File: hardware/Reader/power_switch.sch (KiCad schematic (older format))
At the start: 6 parts

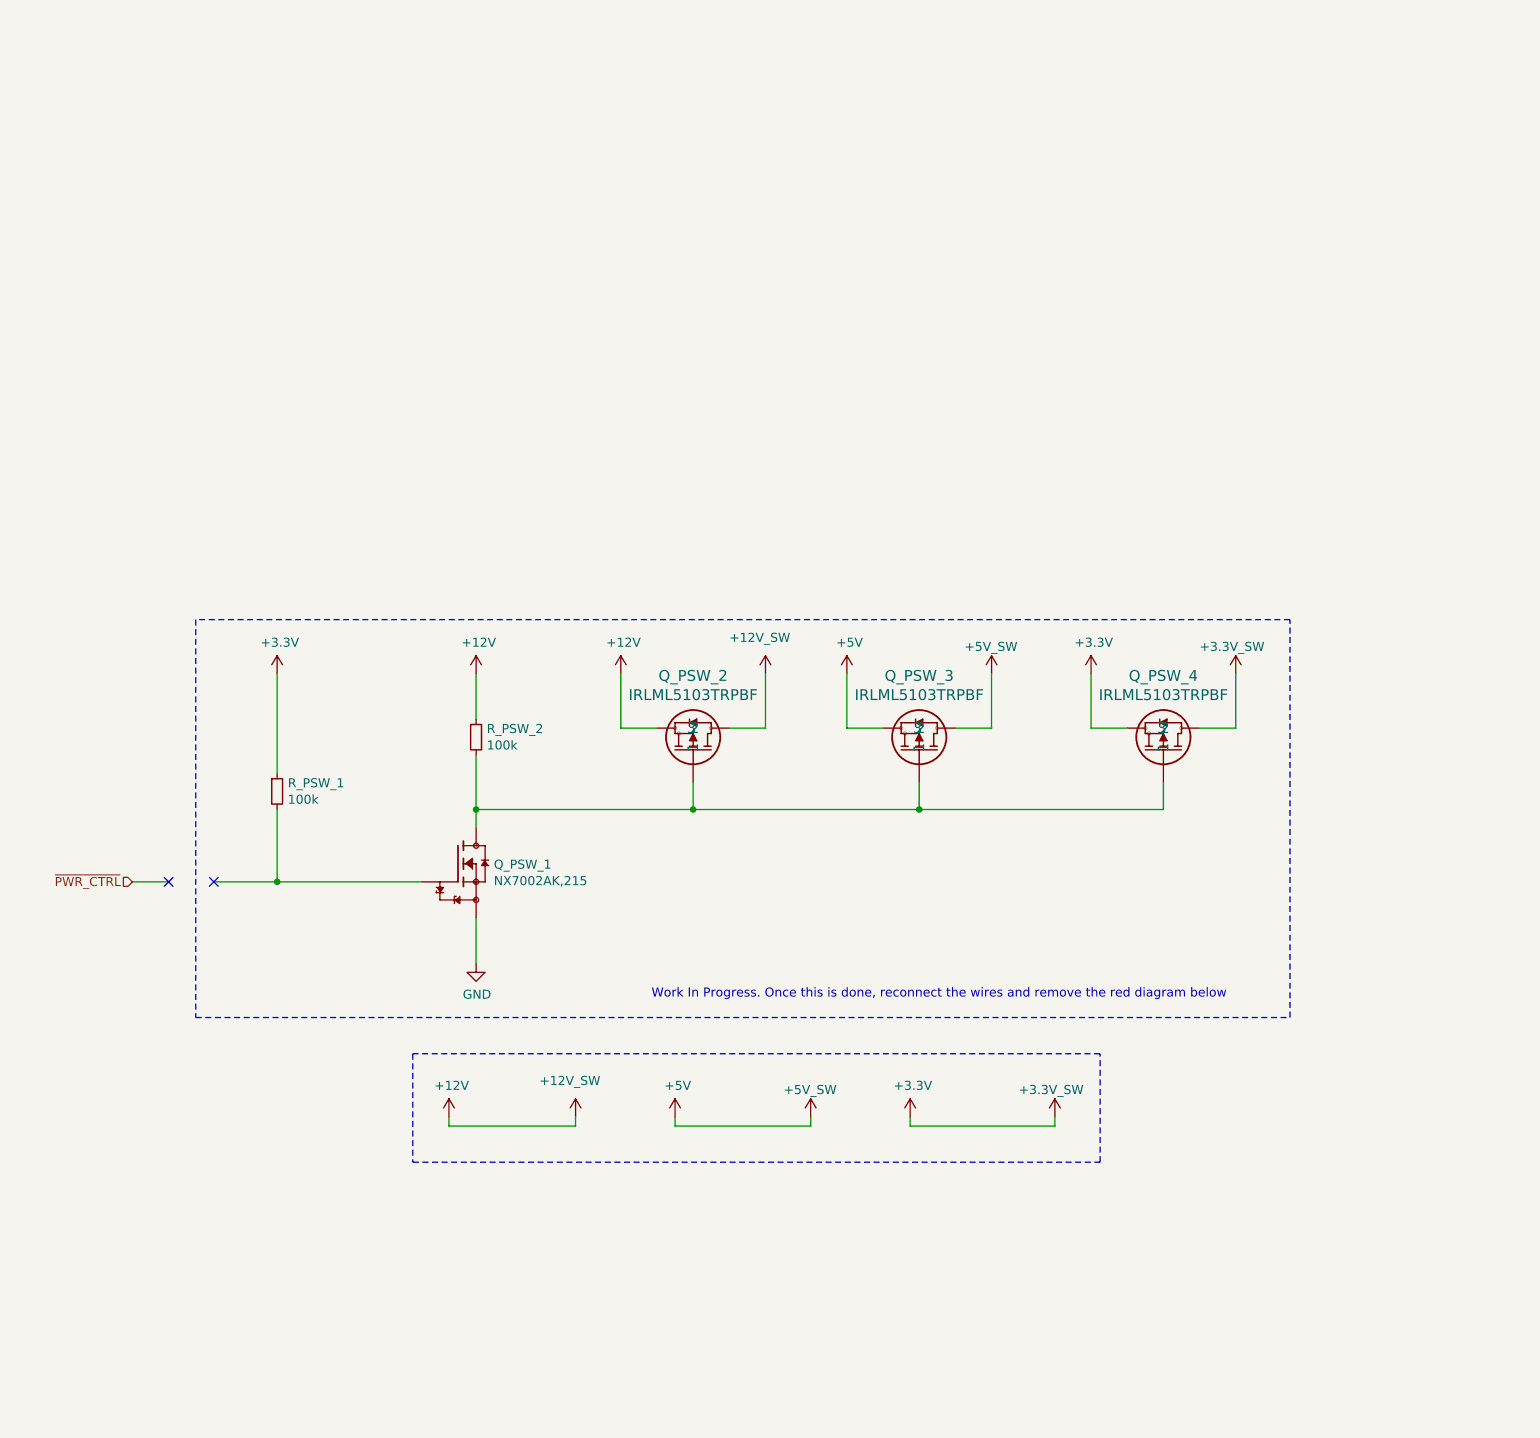
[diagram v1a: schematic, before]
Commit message: Completed Reader schematics for version 0.0.01
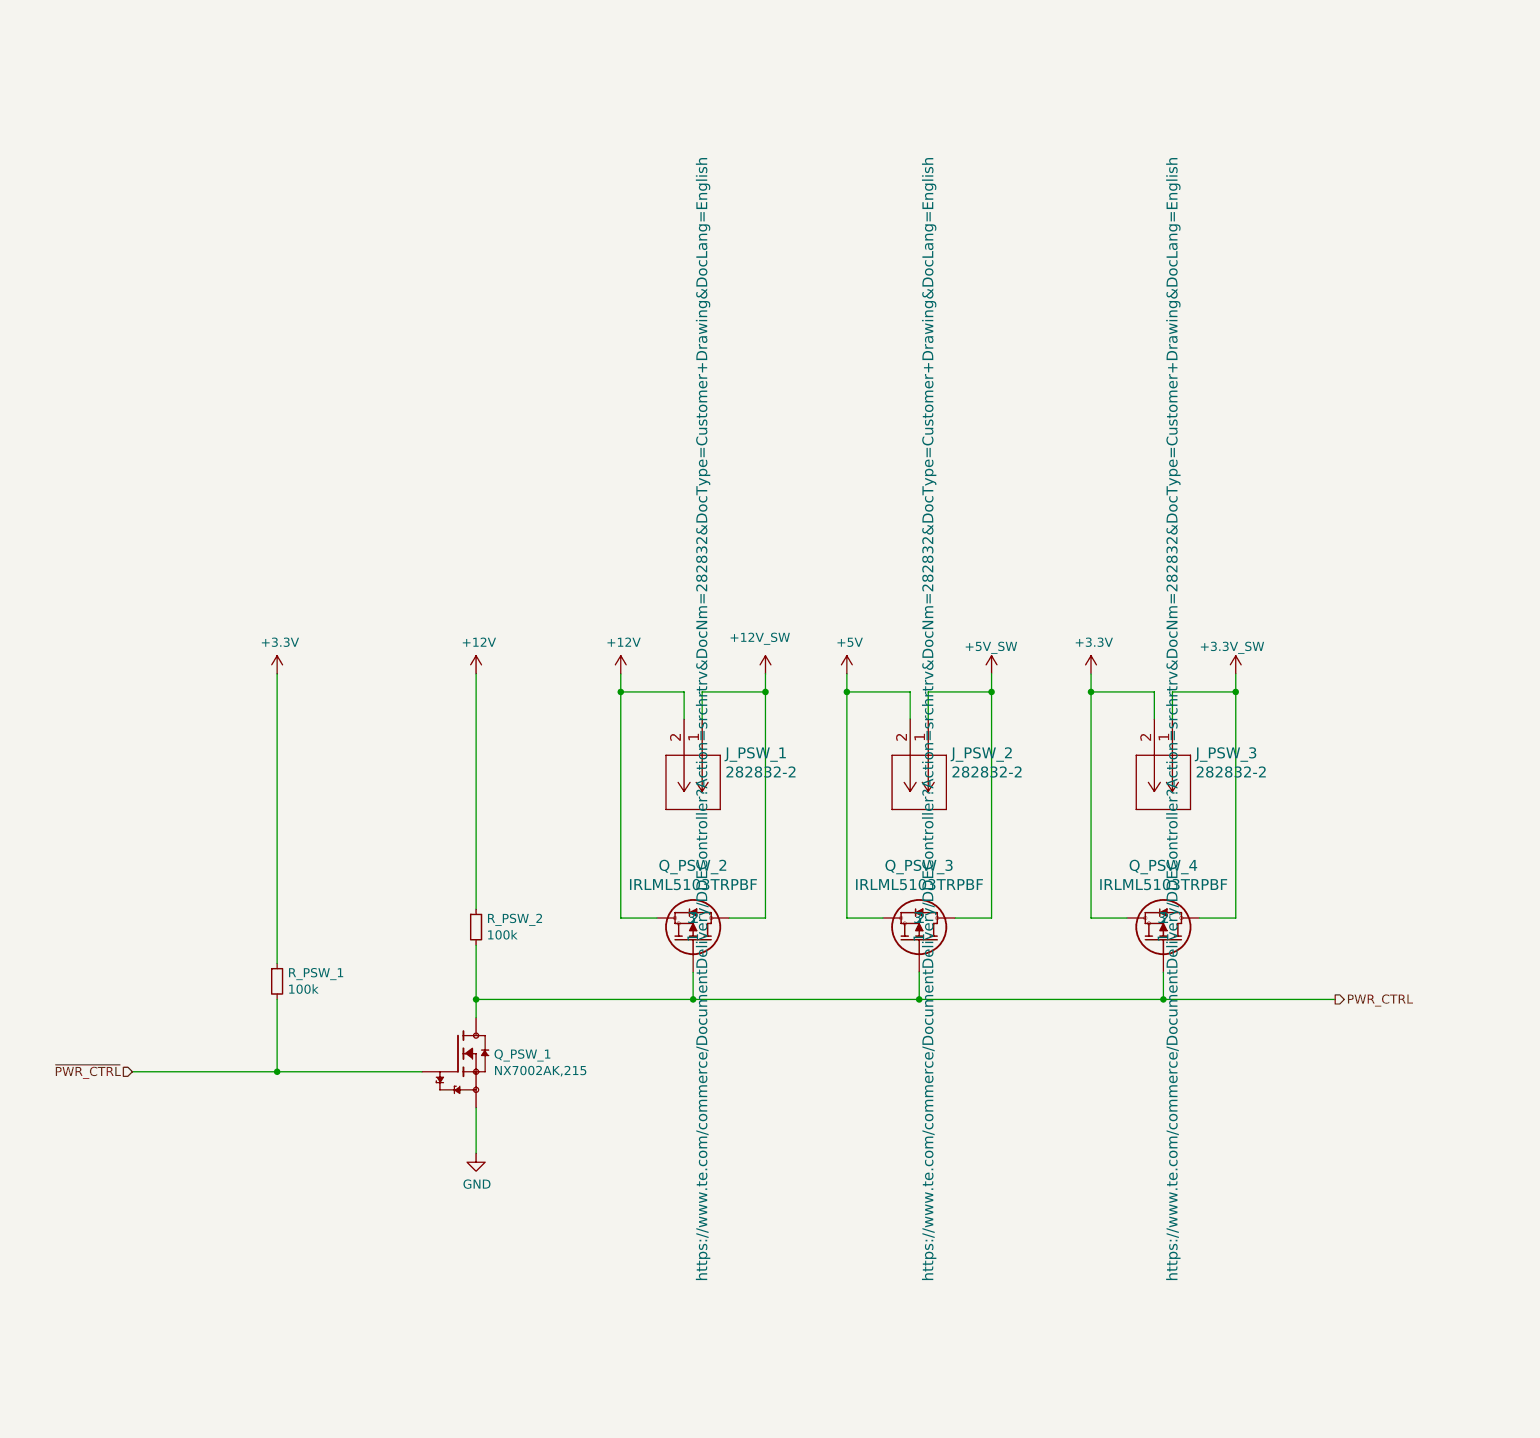
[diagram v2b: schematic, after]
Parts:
- added J_PSW_1, J_PSW_2, J_PSW_3: 282832-2, footprints:282832-2, symbol 2828322:282832-2
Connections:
- net +12V: now also J_PSW_1.2; no longer Q_PSW_2.2
- net +3.3V_SW: now also J_PSW_3.1; no longer Q_PSW_4.3, R_PSW_1.1
- net +5V: now also J_PSW_2.2; no longer Q_PSW_3.2
- net ~PWR_CTRL~: now also Q_PSW_1.1, R_PSW_1.2
- net PWR_CTRL: now reaches Q_PSW_1.3, Q_PSW_2.1, Q_PSW_3.1, Q_PSW_4.1, R_PSW_2.2
- new net +12V_SW: J_PSW_1.1, Q_PSW_2.2
- new net +3V3: J_PSW_3.2, Q_PSW_4.3, R_PSW_1.1
- new net +5V_SW: J_PSW_2.1, Q_PSW_3.2
- no-connect marks 2 -> 0
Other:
- note removed: "Work In Progress. Once this is done, reconnect the wires and remove the red diagram below"
- moved on the sheet: Q_PSW_1, Q_PSW_2, Q_PSW_3, Q_PSW_4, R_PSW_1, R_PSW_2

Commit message: Minor changes to schematic design for clarity. Added important IC datasheets. Exported schematics and rough gerber files
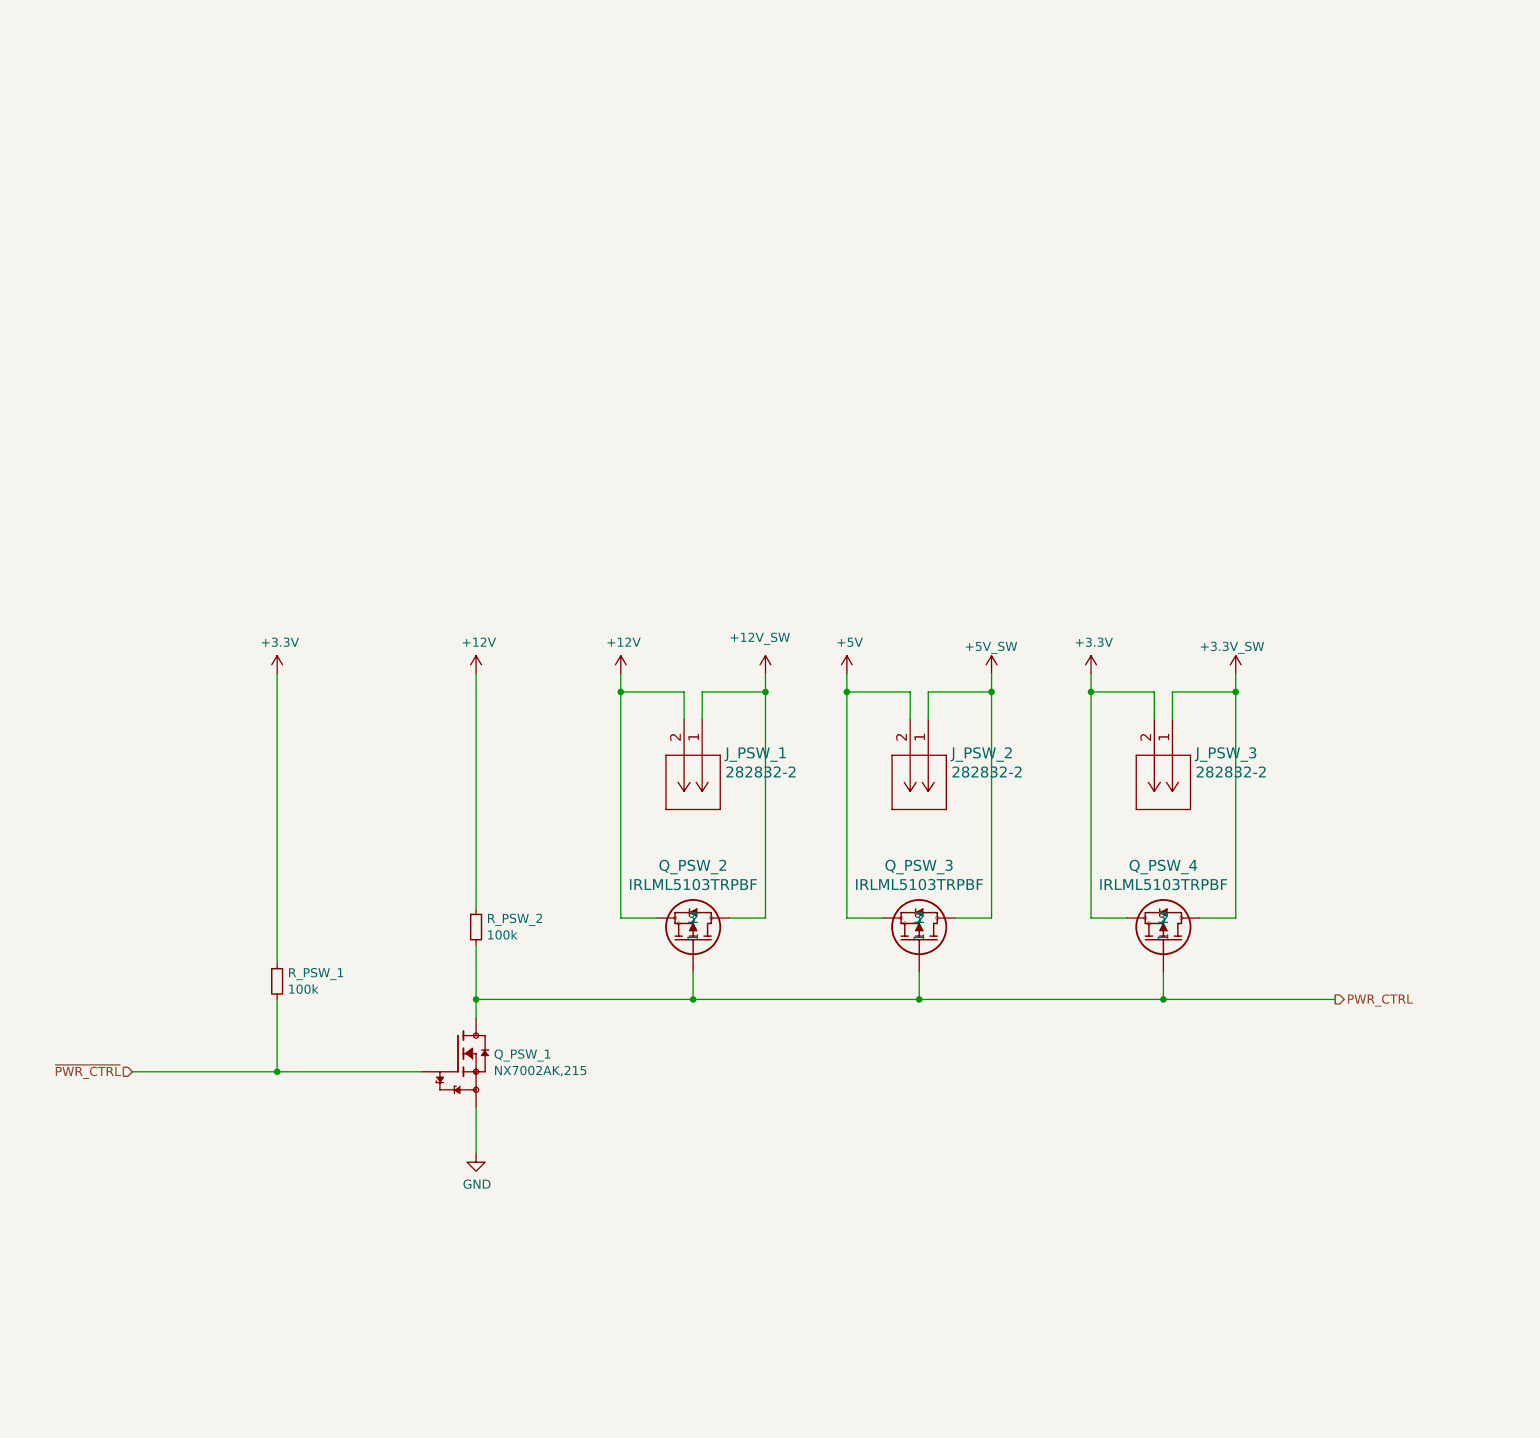
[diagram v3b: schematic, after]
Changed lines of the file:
@@
 F 1 "282832-2" V 4995 2228 60  0000 L CNN
 F 2 "footprints:282832-2" H 5100 2040 60  0001 C CNN
-F 3 "https://www.te.com/commerce/DocumentDelivery/DDEController?Action=srchrtrv&DocNm=282832&DocType=Customer+Drawing&DocLang=English" H 4700 2100 60  0000 C CNN
+F 3 "https://www.te.com/commerce/DocumentDelivery/DDEController?Action=srchrtrv&DocNm=282832&DocType=Customer+Drawing&DocLang=English" H 4700 2100 60  0001 C CNN
 F 4 "282832-2" H 4700 2100 50  0001 C CNN "Part Name"
 	1    4700 2100
@@
 F 1 "282832-2" V 6245 2228 60  0000 L CNN
 F 2 "footprints:282832-2" H 6350 2040 60  0001 C CNN
-F 3 "https://www.te.com/commerce/DocumentDelivery/DDEController?Action=srchrtrv&DocNm=282832&DocType=Customer+Drawing&DocLang=English" H 5950 2100 60  0000 C CNN
+F 3 "https://www.te.com/commerce/DocumentDelivery/DDEController?Action=srchrtrv&DocNm=282832&DocType=Customer+Drawing&DocLang=English" H 5950 2100 60  0001 C CNN
 F 4 "282832-2" H 5950 2100 50  0001 C CNN "Part Name"
 	1    5950 2100
@@
 F 1 "282832-2" V 7595 2228 60  0000 L CNN
 F 2 "footprints:282832-2" H 7700 2040 60  0001 C CNN
-F 3 "https://www.te.com/commerce/DocumentDelivery/DDEController?Action=srchrtrv&DocNm=282832&DocType=Customer+Drawing&DocLang=English" H 7300 2100 60  0000 C CNN
+F 3 "https://www.te.com/commerce/DocumentDelivery/DDEController?Action=srchrtrv&DocNm=282832&DocType=Customer+Drawing&DocLang=English" H 7300 2100 60  0001 C CNN
 F 4 "282832-2" H 7300 2100 50  0001 C CNN "Part Name"
 	1    7300 2100
